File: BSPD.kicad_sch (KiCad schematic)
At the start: 29 parts, among them J1 Screw_Terminal_3.5mm_2, J2 Screw_Terminal_3.5mm_2, J3 Screw_Terminal_3.5mm_3, J4 Screw_Terminal_3.5mm_3, J5 Screw_Terminal_3.5mm_2, J6 Screw_Terminal_3.5mm_2, J7 Screw_Terminal_3.5mm_2, Q3 NPN, U1 LM358, U2 LM358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

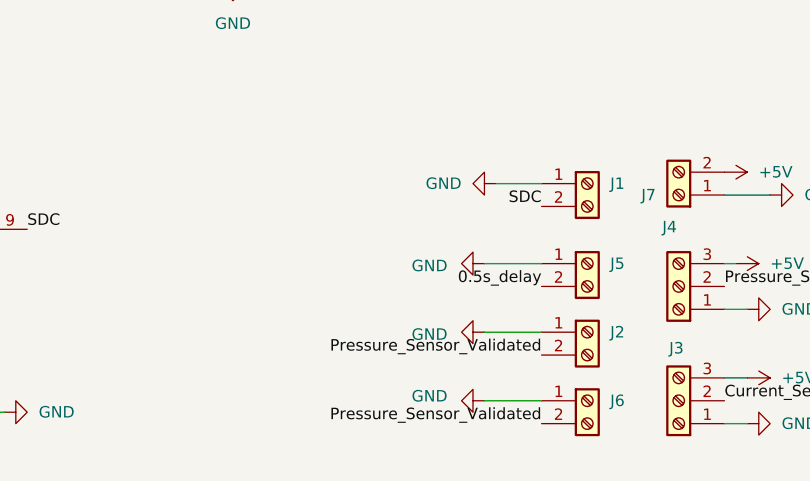
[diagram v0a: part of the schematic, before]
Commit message: updated pcb with better clearance
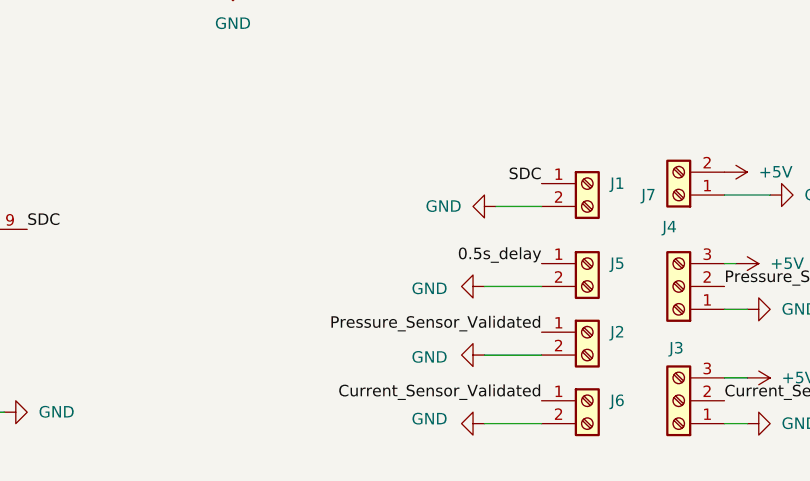
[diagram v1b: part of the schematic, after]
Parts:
- Q3: footprint Package_TO_SOT_THT:TO-92_HandSolder -> Package_TO_SOT_THT:TO-92L_Inline_Wide
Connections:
- net 0.5s_delay: now also J5.1 (Pin_1); no longer J5.2 (Pin_2)
- net Current_Sensor_Validated: now also J6.1 (Pin_1)
- net GND: now also J1.2 (Pin_2), J2.2 (Pin_2), J5.2 (Pin_2), J6.2 (Pin_2); no longer J1.1 (Pin_1), J2.1 (Pin_1), J5.1 (Pin_1), J6.1 (Pin_1)
- net Pressure_Sensor_Validated: now also J2.1 (Pin_1); no longer J2.2 (Pin_2), J6.2 (Pin_2)
- net SDC: now also J1.1 (Pin_1); no longer J1.2 (Pin_2)
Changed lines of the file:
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@@
 	(wire
 		(pts
-			(xy 134.62 173.99) (xy 128.27 173.99)
-		)
-		(stroke
-			(width 0)
-			(type default)
-		)
-	)
-	(wire
-		(pts
 			(xy 224.79 53.34) (xy 231.14 53.34)
 		)
@@
 	(wire
 		(pts
-			(xy 116.84 33.02) (xy 116.84 30.48)
+			(xy 128.27 184.15) (xy 134.62 184.15)
 		)
 		(stroke
@@
 	(wire
 		(pts
-			(xy 90.17 109.22) (xy 90.17 115.57)
+			(xy 116.84 33.02) (xy 116.84 30.48)
 		)
 		(stroke
@@
 	(wire
 		(pts
-			(xy 134.62 181.61) (xy 128.27 181.61)
+			(xy 90.17 109.22) (xy 90.17 115.57)
 		)
 		(stroke
@@
 	(wire
 		(pts
-			(xy 58.42 167.64) (xy 58.42 165.1)
-		)
-		(stroke
-			(width 0)
-			(type default)
-		)
-	)
-	(wire
-		(pts
-			(xy 198.12 146.05) (xy 205.74 146.05)
+			(xy 128.27 176.53) (xy 134.62 176.53)
 		)
 		(stroke
@@
 	(wire
 		(pts
-			(xy 154.94 166.37) (xy 160.02 166.37)
+			(xy 58.42 167.64) (xy 58.42 165.1)
 		)
 		(stroke
@@
 	(wire
 		(pts
-			(xy 219.71 53.34) (xy 219.71 74.93)
+			(xy 198.12 146.05) (xy 205.74 146.05)
 		)
 		(stroke
@@
 	(wire
 		(pts
-			(xy 134.62 189.23) (xy 128.27 189.23)
+			(xy 154.94 166.37) (xy 160.02 166.37)
 		)
 		(stroke
@@
 	(wire
 		(pts
-			(xy 134.62 165.1) (xy 129.54 165.1)
+			(xy 219.71 53.34) (xy 219.71 74.93)
 		)
 		(stroke
@@
 	(wire
 		(pts
+			(xy 128.27 191.77) (xy 134.62 191.77)
+		)
+		(stroke
+			(width 0)
+			(type default)
+		)
+	)
+	(wire
+		(pts
 			(xy 176.53 111.76) (xy 176.53 116.84)
 		)
@@
 		)
 	)
+	(wire
+		(pts
+			(xy 129.54 167.64) (xy 134.62 167.64)
+		)
+		(stroke
+			(width 0)
+			(type default)
+		)
+	)
 	(label "Pressure_Sensor"
 		(at 154.94 176.53 0)
@@
 		)
 	)
-	(label "Pressure_Sensor_Validated"
-		(at 134.62 191.77 180)
-		(effects
-			(font
-				(size 1.27 1.27)
-			)
-			(justify right bottom)
-		)
-	)
 	(label "0.5s_delay"
-		(at 134.62 176.53 180)
+		(at 134.62 173.99 180)
 		(effects
 			(font
@@
 	)
 	(label "Pressure_Sensor_Validated"
-		(at 134.62 184.15 180)
+		(at 134.62 181.61 180)
 		(effects
 			(font
@@
 	)
 	(label "SDC"
-		(at 134.62 167.64 180)
+		(at 134.62 165.1 180)
 		(effects
 			(font
@@
 		)
 	)
+	(label "Current_Sensor_Validated"
+		(at 134.62 189.23 180)
+		(effects
+			(font
+				(size 1.27 1.27)
+			)
+			(justify right bottom)
+		)
+	)
 	(label "Pressure_Sensor_Validated"
 		(at 41.91 170.18 180)
@@
 	(symbol
 		(lib_id "power:GND")
-		(at 128.27 181.61 270)
+		(at 128.27 184.15 270)
 		(unit 1)
 		(exclude_from_sim no)
@@
 		(dnp no)
 		(property "Reference" "#PWR021"
-			(at 121.92 181.61 0)
+			(at 121.92 184.15 0)
 			(effects
 				(font
@@
 		)
 		(property "Value" "GND"
-			(at 122.174 181.864 90)
+			(at 122.174 184.404 90)
 			(effects
 				(font
@@
 		)
 		(property "Footprint" ""
-			(at 128.27 181.61 0)
+			(at 128.27 184.15 0)
 			(effects
 				(font
@@
 		)
 		(property "Datasheet" ""
-			(at 128.27 181.61 0)
+			(at 128.27 184.15 0)
 			(effects
 				(font
@@
 		)
 		(property "Description" "Power symbol creates a global label with name \"GND\" , ground"
-			(at 128.27 181.61 0)
+			(at 128.27 184.15 0)
 			(effects
 				(font
@@
 	(symbol
 		(lib_id "power:GND")
-		(at 129.54 165.1 270)
+		(at 129.54 167.64 270)
 		(unit 1)
 		(exclude_from_sim no)
@@
 		(fields_autoplaced yes)
 		(property "Reference" "#PWR020"
-			(at 123.19 165.1 0)
+			(at 123.19 167.64 0)
 			(effects
 				(font
@@
 		)
 		(property "Value" "GND"
-			(at 125.73 165.0999 90)
+			(at 125.73 167.6399 90)
 			(effects
 				(font
@@
 		)
 		(property "Footprint" ""
-			(at 129.54 165.1 0)
+			(at 129.54 167.64 0)
 			(effects
 				(font
@@
 		)
 		(property "Datasheet" ""
-			(at 129.54 165.1 0)
+			(at 129.54 167.64 0)
 			(effects
 				(font
@@
 		)
 		(property "Description" "Power symbol creates a global label with name \"GND\" , ground"
-			(at 129.54 165.1 0)
+			(at 129.54 167.64 0)
 			(effects
 				(font
@@
 	(symbol
 		(lib_id "power:GND")
-		(at 128.27 173.99 270)
+		(at 128.27 176.53 270)
 		(unit 1)
 		(exclude_from_sim no)
@@
 		(dnp no)
 		(property "Reference" "#PWR022"
-			(at 121.92 173.99 0)
+			(at 121.92 176.53 0)
 			(effects
 				(font
@@
 		)
 		(property "Value" "GND"
-			(at 122.174 174.244 90)
+			(at 122.174 176.784 90)
 			(effects
 				(font
@@
 		)
 		(property "Footprint" ""
-			(at 128.27 173.99 0)
+			(at 128.27 176.53 0)
 			(effects
 				(font
@@
 		)
 		(property "Datasheet" ""
-			(at 128.27 173.99 0)
+			(at 128.27 176.53 0)
 			(effects
 				(font
@@
 		)
 		(property "Description" "Power symbol creates a global label with name \"GND\" , ground"
-			(at 128.27 173.99 0)
+			(at 128.27 176.53 0)
 			(effects
 				(font
@@
 	(symbol
 		(lib_id "power:GND")
-		(at 128.27 189.23 270)
+		(at 128.27 191.77 270)
 		(unit 1)
 		(exclude_from_sim no)
@@
 		(dnp no)
 		(property "Reference" "#PWR031"
-			(at 121.92 189.23 0)
+			(at 121.92 191.77 0)
 			(effects
 				(font
@@
 		)
 		(property "Value" "GND"
-			(at 122.174 188.722 90)
+			(at 122.174 191.262 90)
 			(effects
 				(font
@@
 		)
 		(property "Footprint" ""
-			(at 128.27 189.23 0)
+			(at 128.27 191.77 0)
 			(effects
 				(font
@@
 		)
 		(property "Datasheet" ""
-			(at 128.27 189.23 0)
+			(at 128.27 191.77 0)
 			(effects
 				(font
@@
 		)
 		(property "Description" "Power symbol creates a global label with name \"GND\" , ground"
-			(at 128.27 189.23 0)
+			(at 128.27 191.77 0)
 			(effects
 				(font
@@
 			)
 		)
-		(property "Footprint" "Package_TO_SOT_THT:TO-92_HandSolder"
+		(property "Footprint" "Package_TO_SOT_THT:TO-92L_Inline_Wide"
 			(at 271.78 59.69 0)
 			(effects
